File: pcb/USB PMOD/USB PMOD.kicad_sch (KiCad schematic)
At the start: 6 parts, among them J1 USB_B_Mini, J2 929836-08-06-RK

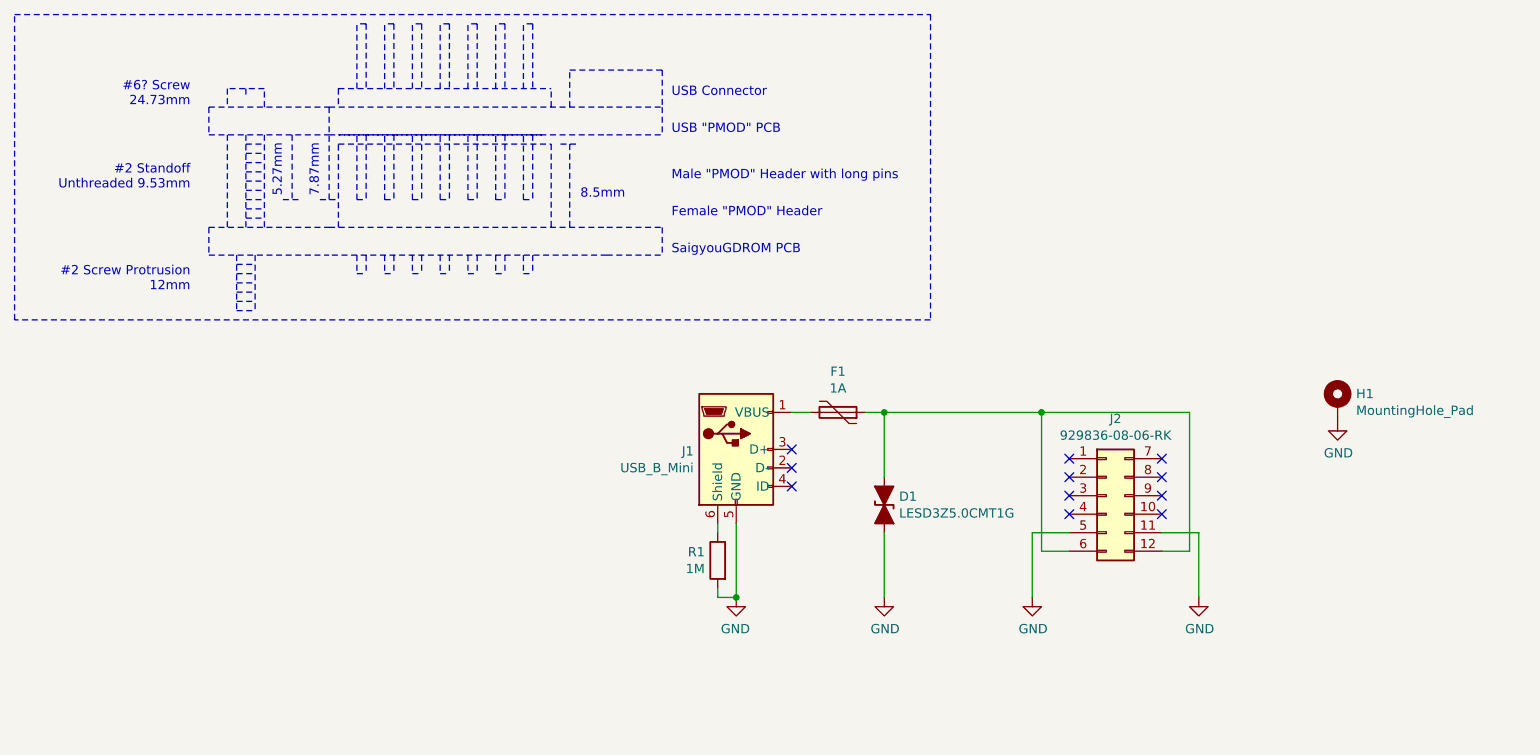
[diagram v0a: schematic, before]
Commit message: Deleting backup files from git repository, and updating the USB PMOD board to latest nightly build.
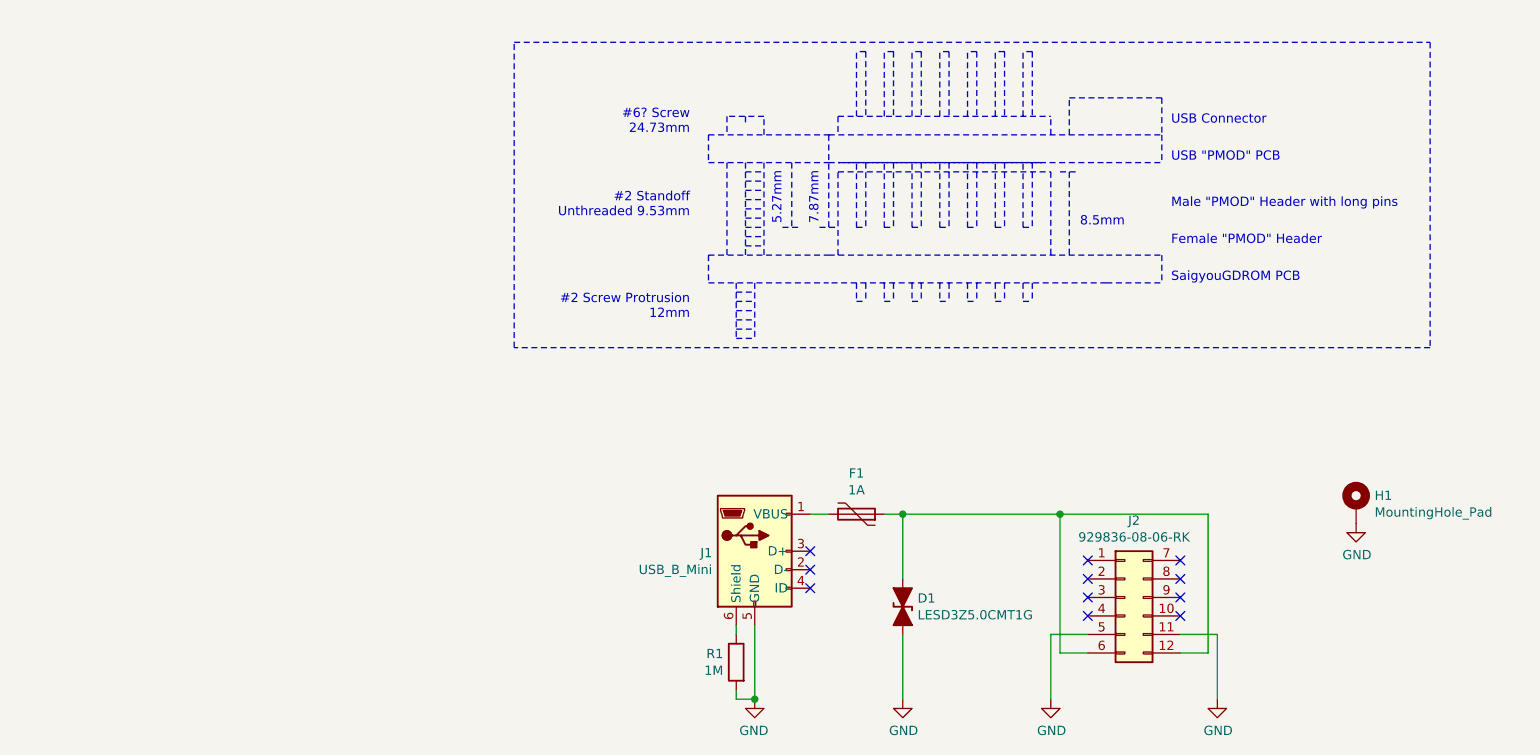
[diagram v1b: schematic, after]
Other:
- moved on the sheet: D1, F1, H1, J1, J2, R1
